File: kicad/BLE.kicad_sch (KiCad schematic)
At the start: 1 part

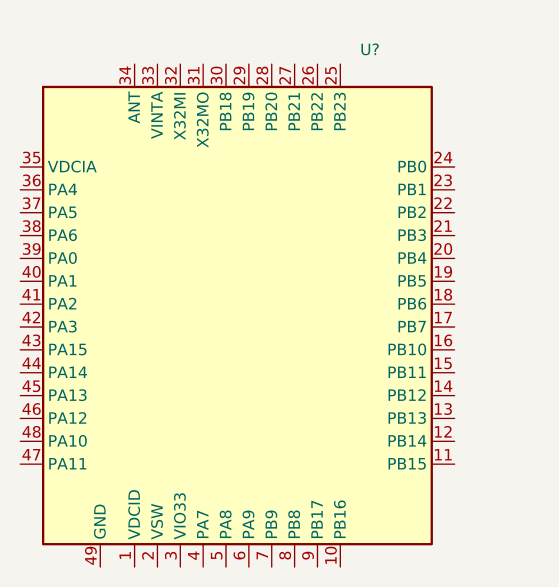
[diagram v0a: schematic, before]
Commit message: fixed issues with footprints and symbols, minor connections drawn | TODO: DC-DC regulator empty footprint
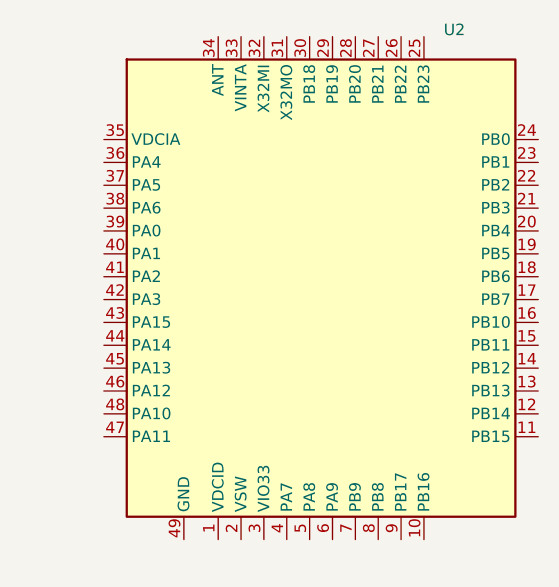
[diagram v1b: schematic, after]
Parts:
- removed U?: ~, wireless_testboard:CH582-QFN-48-1EP_5x5mm_P0.35mm_EP3.7x3.7mm, symbol wireless_testboard:CH582M
- added U2: ~, hw_wireless_testboard:CH582-QFN-48-1EP_5x5mm_P0.35mm_EP3.7x3.7mm, symbol hw_wireless_testboard:CH582M
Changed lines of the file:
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@@
 	(paper "A4")
 	(symbol
-		(lib_id "wireless_testboard:CH582M")
-		(at 88.5 90.68 0)
+		(lib_id "hw_wireless_testboard:CH582M")
+		(at 97.79 87.63 0)
 		(unit 1)
 		(exclude_from_sim no)
@@
 		(dnp no)
 		(fields_autoplaced yes)
-		(property "Reference" "U?"
-			(at 101.2541 60.64 0)
+		(property "Reference" "U2"
+			(at 110.5441 58.42 0)
 			(effects
 				(font
@@
 		)
 		(property "Value" "~"
-			(at 101.2541 63.18 0)
+			(at 110.5441 59.69 0)
 			(effects
 				(font
@@
 			)
 		)
-		(property "Footprint" "wireless_testboard:CH582-QFN-48-1EP_5x5mm_P0.35mm_EP3.7x3.7mm"
-			(at 88.5 90.68 0)
+		(property "Footprint" "hw_wireless_testboard:CH582-QFN-48-1EP_5x5mm_P0.35mm_EP3.7x3.7mm"
+			(at 97.79 87.63 0)
 			(effects
 				(font
@@
 			)
 		)
-		(property "Datasheet" ""
-			(at 88.5 90.68 0)
+		(property "Datasheet" "https://wmsc.lcsc.com/wmsc/upload/file/pdf/v2/lcsc/2403131113_WCH-Jiangsu-Qin-Heng-CH582M_C2920766.pdf"
+			(at 97.79 87.63 0)
 			(effects
 				(font
@@
 		)
 		(property "Description" ""
-			(at 88.5 90.68 0)
+			(at 97.79 87.63 0)
 			(effects
 				(font
@@
 			)
 		)
-		(pin "24"
+		(property "jlcpcb" "C2920766"
+			(at 97.79 87.63 0)
+			(effects
+				(font
+					(size 1.27 1.27)
+				)
+				(hide yes)
+			)
 		)
-		(pin "49"
+		(property "MFR.Part" "CH582M"
+			(at 97.79 87.63 0)
+			(effects
+				(font
+					(size 1.27 1.27)
+				)
+				(hide yes)
+			)
 		)
 		(pin "5"
 		)
-		(pin "38"
+		(pin "43"
 		)
-		(pin "37"
-		)
-		(pin "6"
+		(pin "45"
 		)
 		(pin "26"
 		)
-		(pin "7"
+		(pin "46"
 		)
-		(pin "8"
+		(pin "47"
 		)
-		(pin "41"
+		(pin "11"
 		)
-		(pin "42"
+		(pin "1"
 		)
-		(pin "43"
+		(pin "32"
 		)
 		(pin "40"
 		)
-		(pin "22"
+		(pin "20"
 		)
-		(pin "21"
+		(pin "33"
 		)
-		(pin "47"
+		(pin "38"
 		)
-		(pin "12"
+		(pin "23"
 		)
-		(pin "15"
+		(pin "18"
 		)
-		(pin "13"
-		)
-		(pin "14"
-		)
-		(pin "11"
+		(pin "36"
 		)
 		(pin "10"
-		)
-		(pin "1"
-		)
-		(pin "36"
 		)
 		(pin "29"
@@
 		(pin "48"
 		)
-		(pin "16"
+		(pin "15"
 		)
-		(pin "18"
+		(pin "3"
+		)
+		(pin "9"
+		)
+		(pin "25"
+		)
+		(pin "35"
+		)
+		(pin "19"
+		)
+		(pin "30"
+		)
+		(pin "31"
+		)
+		(pin "6"
 		)
 		(pin "39"
 		)
-		(pin "35"
+		(pin "27"
+		)
+		(pin "24"
+		)
+		(pin "7"
+		)
+		(pin "34"
+		)
+		(pin "42"
+		)
+		(pin "8"
+		)
+		(pin "49"
+		)
+		(pin "4"
+		)
+		(pin "14"
+		)
+		(pin "12"
+		)
+		(pin "13"
+		)
+		(pin "37"
 		)
 		(pin "17"
 		)
-		(pin "20"
+		(pin "21"
 		)
-		(pin "34"
+		(pin "44"
 		)
-		(pin "31"
-		)
-		(pin "46"
-		)
-		(pin "32"
-		)
-		(pin "23"
-		)
-		(pin "45"
-		)
-		(pin "25"
+		(pin "16"
 		)
 		(pin "2"
 		)
-		(pin "4"
-		)
-		(pin "30"
-		)
-		(pin "33"
-		)
 		(pin "28"
 		)
-		(pin "3"
+		(pin "41"
 		)
-		(pin "19"
-		)
-		(pin "27"
-		)
-		(pin "44"
-		)
-		(pin "9"
+		(pin "22"
 		)
 		(instances
 			(project ""
 				(path "/601a88ea-2da7-4ec4-b637-f587eb4ba821/50fdb7d1-4569-4c52-8829-8f3c547b35ac"
-					(reference "U?")
+					(reference "U2")
 					(unit 1)
 				)

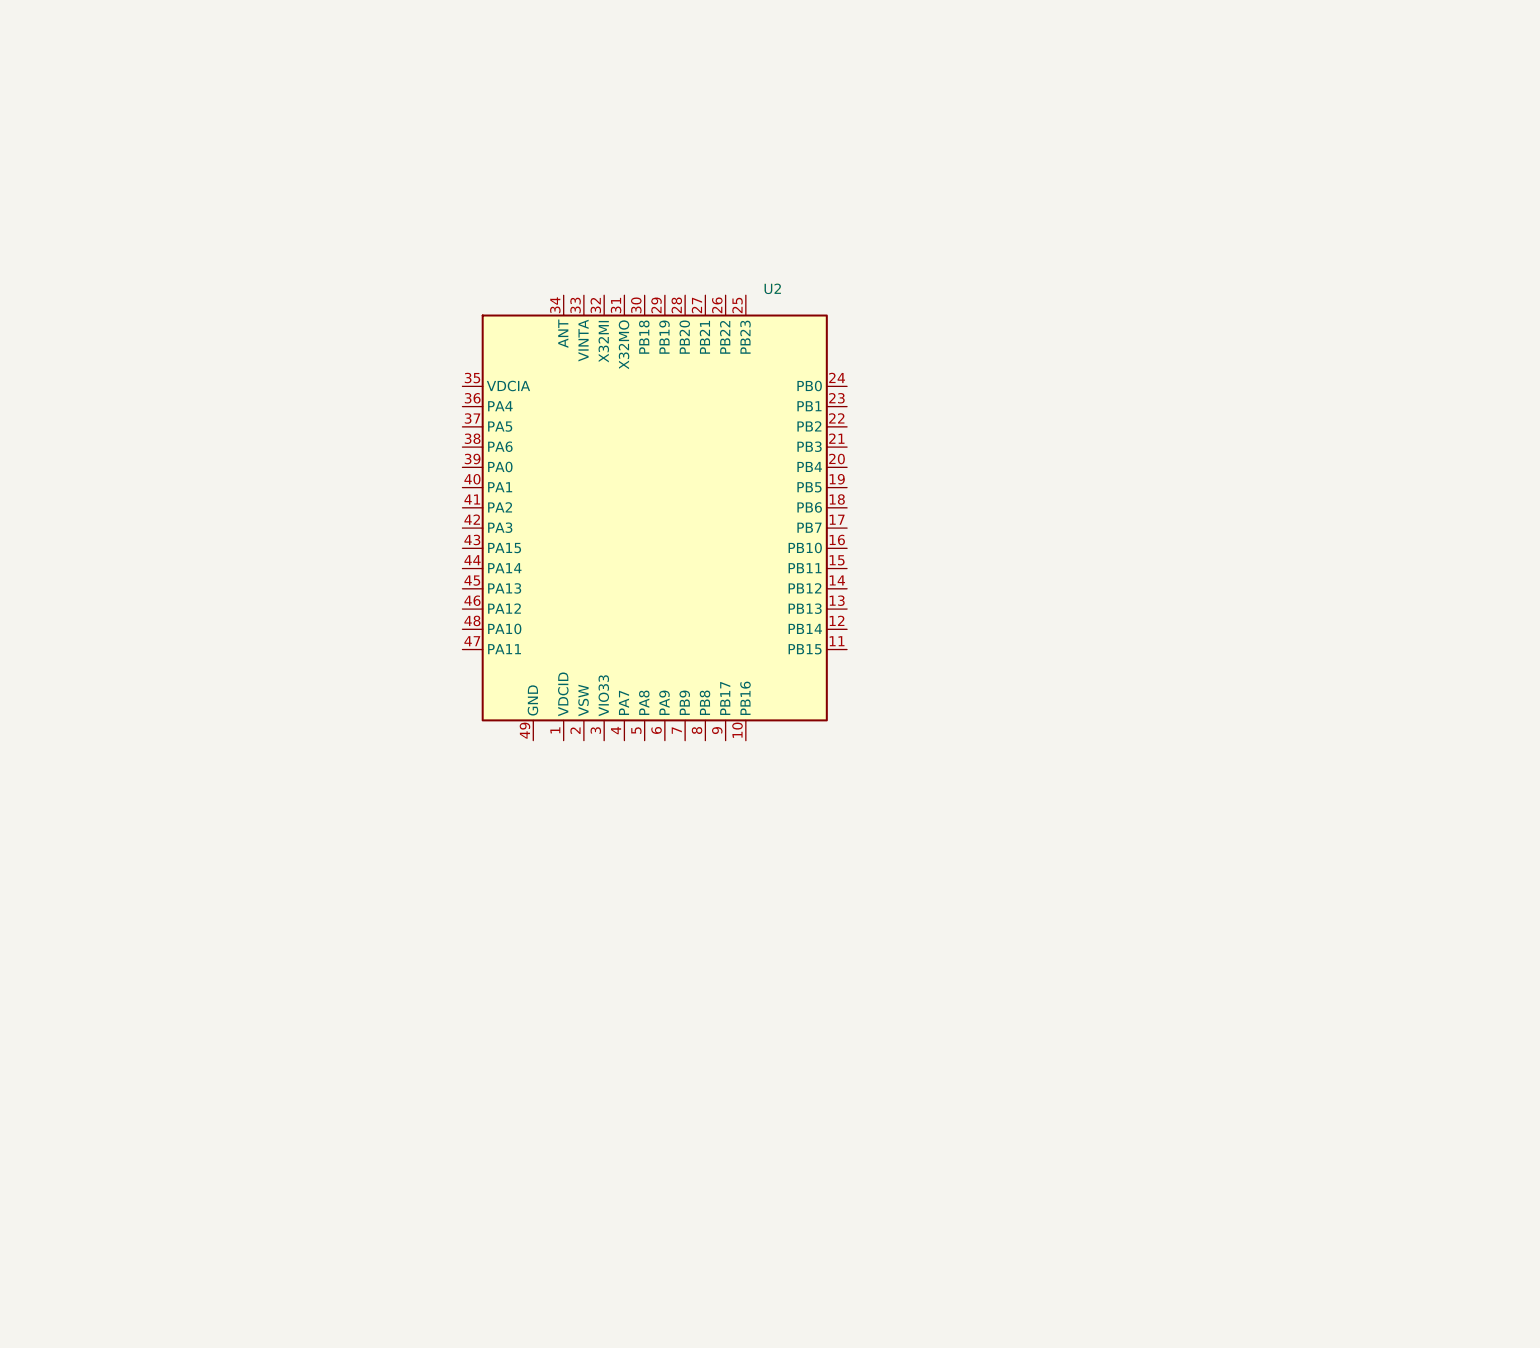
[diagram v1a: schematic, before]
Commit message: finished bluetooth schematic apart from anteantenna-design, WiFi design started
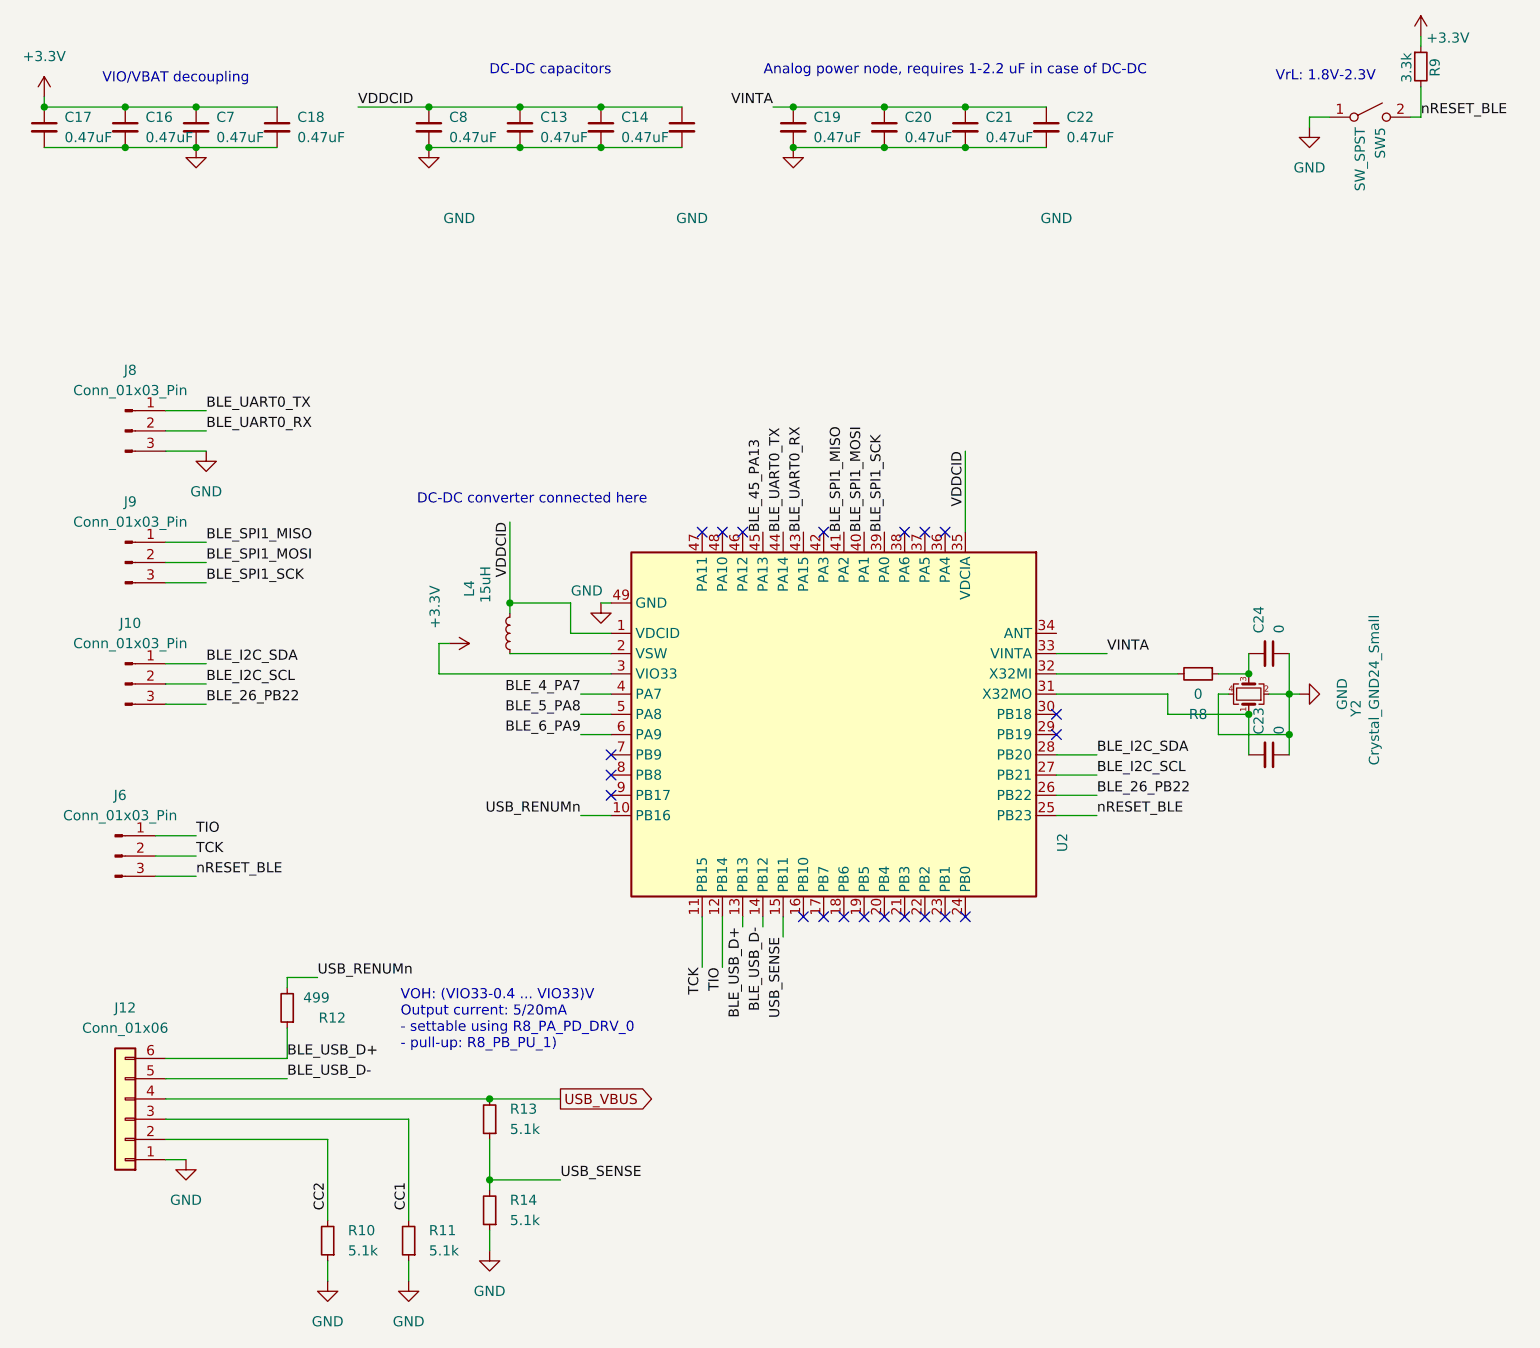
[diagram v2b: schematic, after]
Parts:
- added C13, C14, C15, C16, C17, C18, C19, C20, C21, C22, C7, C8: 0.47uF, symbol Device:C_Small
- added C23, C24: 0, symbol Device:C_Small
- added J10, J6, J8, J9: Conn_01x03_Pin, symbol Connector:Conn_01x03_Pin
- added J12: Conn_01x06, symbol Connector_Generic:Conn_01x06
- added L4: 15uH, symbol Device:L_Small
- added R10, R11, R13, R14: 5.1k, Resistor_SMD:R_0805_2012Metric, symbol Device:R_Small
- added R12: 499, Resistor_SMD:R_0402_1005Metric, symbol Device:R_Small
- added R8: 0, Resistor_SMD:R_0402_1005Metric_Pad0.72x0.64mm_HandSolder, symbol Device:R_Small
- added R9: 3.3k, symbol Device:R_Small
- added SW5: SW_SPST, symbol Switch:SW_SPST
- added Y2: Crystal_GND24_Small, Crystal:Crystal_SMD_3225-4Pin_3.2x2.5mm_HandSoldering, symbol Device:Crystal_GND24_Small
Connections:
- net VDDCID: now reaches U2.1 (VDCID)
- net VDDCID: now also U2.35 (VDCIA), C13.1, C14.1, C15.1, C8.1, L4.2
- net USB_RENUMn: now reaches U2.10 (PB16)
- net USB_RENUMn: now also R12.2
- net TCK: now reaches U2.11 (PB15)
- net TCK: now also J6.2 (Pin_2)
- net TIO: now reaches U2.12 (PB14)
- net TIO: now also J6.1 (Pin_1)
- net BLE_USB_D+: now reaches U2.13 (PB13)
- net BLE_USB_D+: now also J12.6 (Pin_6), R12.1
- net BLE_USB_D-: now reaches U2.14 (PB12)
- net BLE_USB_D-: now also J12.5 (Pin_5)
- net USB_SENSE: now reaches U2.15 (PB11)
- net USB_SENSE: now also R13.1, R14.2
- net at U2.2 (VSW): now also L4.1
- net nRESET_BLE: now reaches U2.25 (PB23)
- net nRESET_BLE: now also J6.3 (Pin_3), R9.2, SW5.2 (B)
- net BLE_26_PB22: now reaches U2.26 (PB22)
- net BLE_26_PB22: now also J10.3 (Pin_3)
- net BLE_I2C_SCL: now reaches U2.27 (PB21)
- net BLE_I2C_SCL: now also J10.2 (Pin_2)
- net BLE_I2C_SDA: now reaches U2.28 (PB20)
- net BLE_I2C_SDA: now also J10.1 (Pin_1)
- net +3.3V: now reaches U2.3 (VIO33)
- net +3.3V: now also C16.1, C17.1, C18.1, C7.1, R9.1
- net at U2.31 (X32MO): now also C23.2, Y2.1
- net at U2.32 (X32MI): now also R8.2
- net VINTA: now reaches U2.33 (VINTA)
- net VINTA: now also C19.1, C20.1, C21.1, C22.1
- net BLE_SPI1_SCK: now reaches U2.39 (PA0)
- net BLE_SPI1_SCK: now also J9.3 (Pin_3)
- net BLE_4_PA7: now reaches U2.4 (PA7)
- net BLE_SPI1_MOSI: now reaches U2.40 (PA1)
- net BLE_SPI1_MOSI: now also J9.2 (Pin_2)
- net BLE_SPI1_MISO: now reaches U2.41 (PA2)
- net BLE_SPI1_MISO: now also J9.1 (Pin_1)
- net BLE_UART0_RX: now reaches U2.43 (PA15)
- net BLE_UART0_RX: now also J8.2 (Pin_2)
- net BLE_UART0_TX: now reaches U2.44 (PA14)
- net BLE_UART0_TX: now also J8.1 (Pin_1)
- net BLE_45_PA13: now reaches U2.45 (PA13)
- net GND: now reaches U2.49 (GND)
- net GND: now also C13.2, C14.2, C15.2, C16.2, C17.2, C18.2, C19.2, C20.2, C21.2, C22.2, C23.1, C24.1, C7.2, C8.2, J12.1 (Pin_1), J8.3 (Pin_3), R10.1, R11.1, R14.1, SW5.1 (A), Y2.2, Y2.4
- net BLE_5_PA8: now reaches U2.5 (PA8)
- net BLE_6_PA9: now reaches U2.6 (PA9)
- new net: C24.2, R8.1, Y2.3
- new net CC1: J12.3 (Pin_3), R11.2
- new net CC2: J12.2 (Pin_2), R10.2
- new net USB_VBUS: J12.4 (Pin_4), R13.2
- no-connect marks 0 -> 21
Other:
- note added: "Analog power node, requires 1-2.2 uF in case of DC-DC"
- note added: "DC-DC capacitors"
- note added: "DC-DC converter connected here"
- note added: "VIO/VBAT decoupling"
- note added: "VOH: (VIO33-0.4 ... VIO33)V Output current: 5/20mA - settable using R8_PA_PD_DRV_0 - pull-up: R8_PB_PU_1)"
- note added: "VrL: 1.8V-2.3V"
- moved on the sheet: U2
